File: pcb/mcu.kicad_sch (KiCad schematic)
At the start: 19 parts, among them J3 ESPPROG, J4 USB_C_Receptacle_USB2.0_14P, SW1 RST_SW, SW2 BOOT_SW, U4 ESP32-C6-MINI-1, U6 TLV803S, U7 W5500

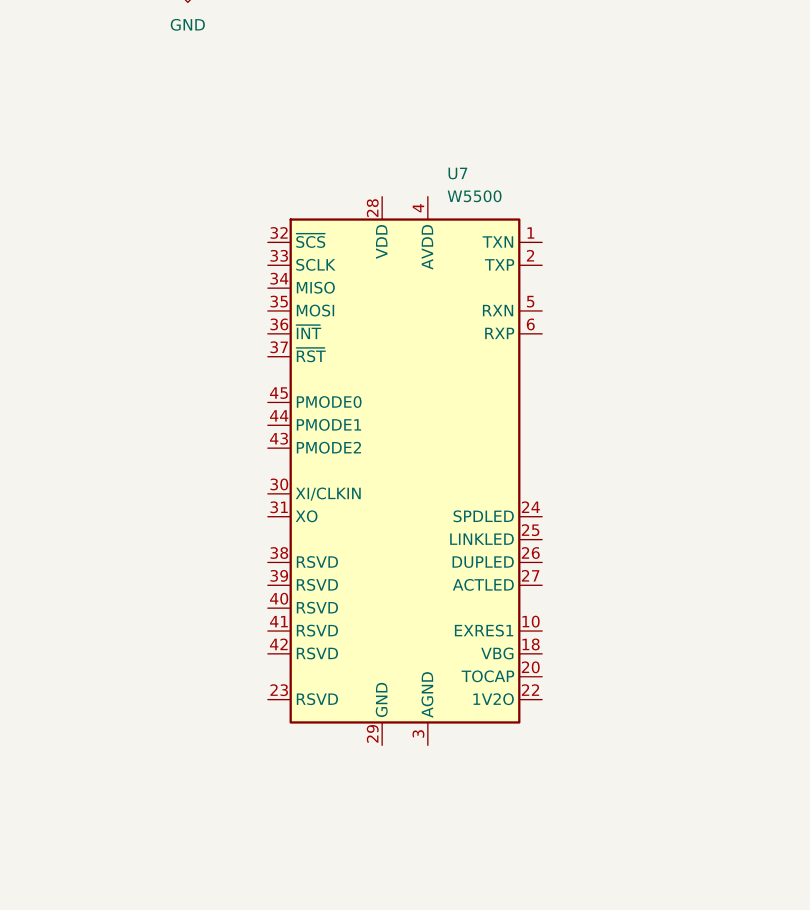
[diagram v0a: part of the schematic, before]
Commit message: feat: add W5500 ethernet controller
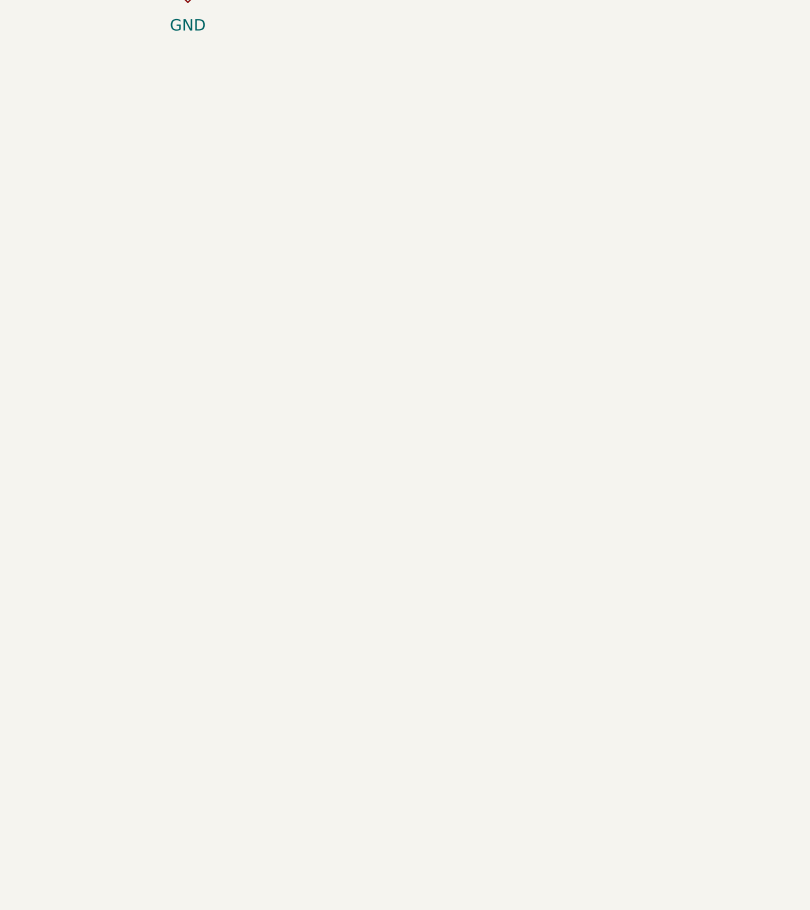
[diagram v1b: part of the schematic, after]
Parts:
- removed U7: W5500, Package_QFP:LQFP-48_7x7mm_P0.5mm, symbol Interface_Ethernet:W5500
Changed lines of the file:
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@@
-	)
-	(symbol
-		(lib_id "Interface_Ethernet:W5500")
-		(at 120.65 106.68 0)
-		(unit 1)
-		(body_style 1)
-		(exclude_from_sim no)
-		(in_bom yes)
-		(on_board yes)
-		(in_pos_files yes)
-		(dnp no)
-		(fields_autoplaced yes)
-		(property "Reference" "U7"
-			(at 125.3333 73.66 0)
-			(show_name no)
-			(do_not_autoplace no)
-			(effects
-				(font
-					(size 1.27 1.27)
-				)
-				(justify left)
-			)
-		)
-		(property "Value" "W5500"
-			(at 125.3333 76.2 0)
-			(show_name no)
-			(do_not_autoplace no)
-			(effects
-				(font
-					(size 1.27 1.27)
-				)
-				(justify left)
-			)
-		)
-		(property "Footprint" "Package_QFP:LQFP-48_7x7mm_P0.5mm"
-			(at 120.65 64.77 0)
-			(hide yes)
-			(show_name no)
-			(do_not_autoplace no)
-			(effects
-				(font
-					(size 1.27 1.27)
-				)
-			)
-		)
-		(property "Datasheet" "http://wizwiki.net/wiki/lib/exe/fetch.php/products:w5500:w5500_ds_v109e.pdf"
-			(at 120.65 81.28 0)
-			(hide yes)
-			(show_name no)
-			(do_not_autoplace no)
-			(effects
-				(font
-					(size 1.27 1.27)
-				)
-			)
-		)
-		(property "Description" "10/100Mb SPI Ethernet controller with TCP/IP stack, LQFP-48"
-			(at 120.65 106.68 0)
-			(hide yes)
-			(show_name no)
-			(do_not_autoplace no)
-			(effects
-				(font
-					(size 1.27 1.27)
-				)
-			)
-		)
-		(pin "2"
-		)
-		(pin "9"
-		)
-		(pin "38"
-		)
-		(pin "5"
-		)
-		(pin "23"
-		)
-		(pin "10"
-		)
-		(pin "26"
-		)
-		(pin "24"
-		)
-		(pin "7"
-		)
-		(pin "40"
-		)
-		(pin "8"
-		)
-		(pin "29"
-		)
-		(pin "16"
-		)
-		(pin "13"
-		)
-		(pin "25"
-		)
-		(pin "12"
-		)
-		(pin "33"
-		)
-		(pin "18"
-		)
-		(pin "14"
-		)
-		(pin "22"
-		)
-		(pin "35"
-		)
-		(pin "32"
-		)
-		(pin "46"
-		)
-		(pin "19"
-		)
-		(pin "20"
-		)
-		(pin "3"
-		)
-		(pin "30"
-		)
-		(pin "28"
-		)
-		(pin "37"
-		)
-		(pin "11"
-		)
-		(pin "17"
-		)
-		(pin "42"
-		)
-		(pin "39"
-		)
-		(pin "6"
-		)
-		(pin "43"
-		)
-		(pin "31"
-		)
-		(pin "44"
-		)
-		(pin "27"
-		)
-		(pin "15"
-		)
-		(pin "34"
-		)
-		(pin "48"
-		)
-		(pin "47"
-		)
-		(pin "1"
-		)
-		(pin "41"
-		)
-		(pin "45"
-		)
-		(pin "21"
-		)
-		(pin "36"
-		)
-		(pin "4"
-		)
-		(instances
-			(project "EveningStar"
-				(path "/4c61f5a2-f8d4-462a-9bc3-d74437d30372/83e90eda-4c3c-4f86-9f5b-c472ac53896a"
-					(reference "U7")
-					(unit 1)
-				)
-			)
-		)
 	)
 	(symbol

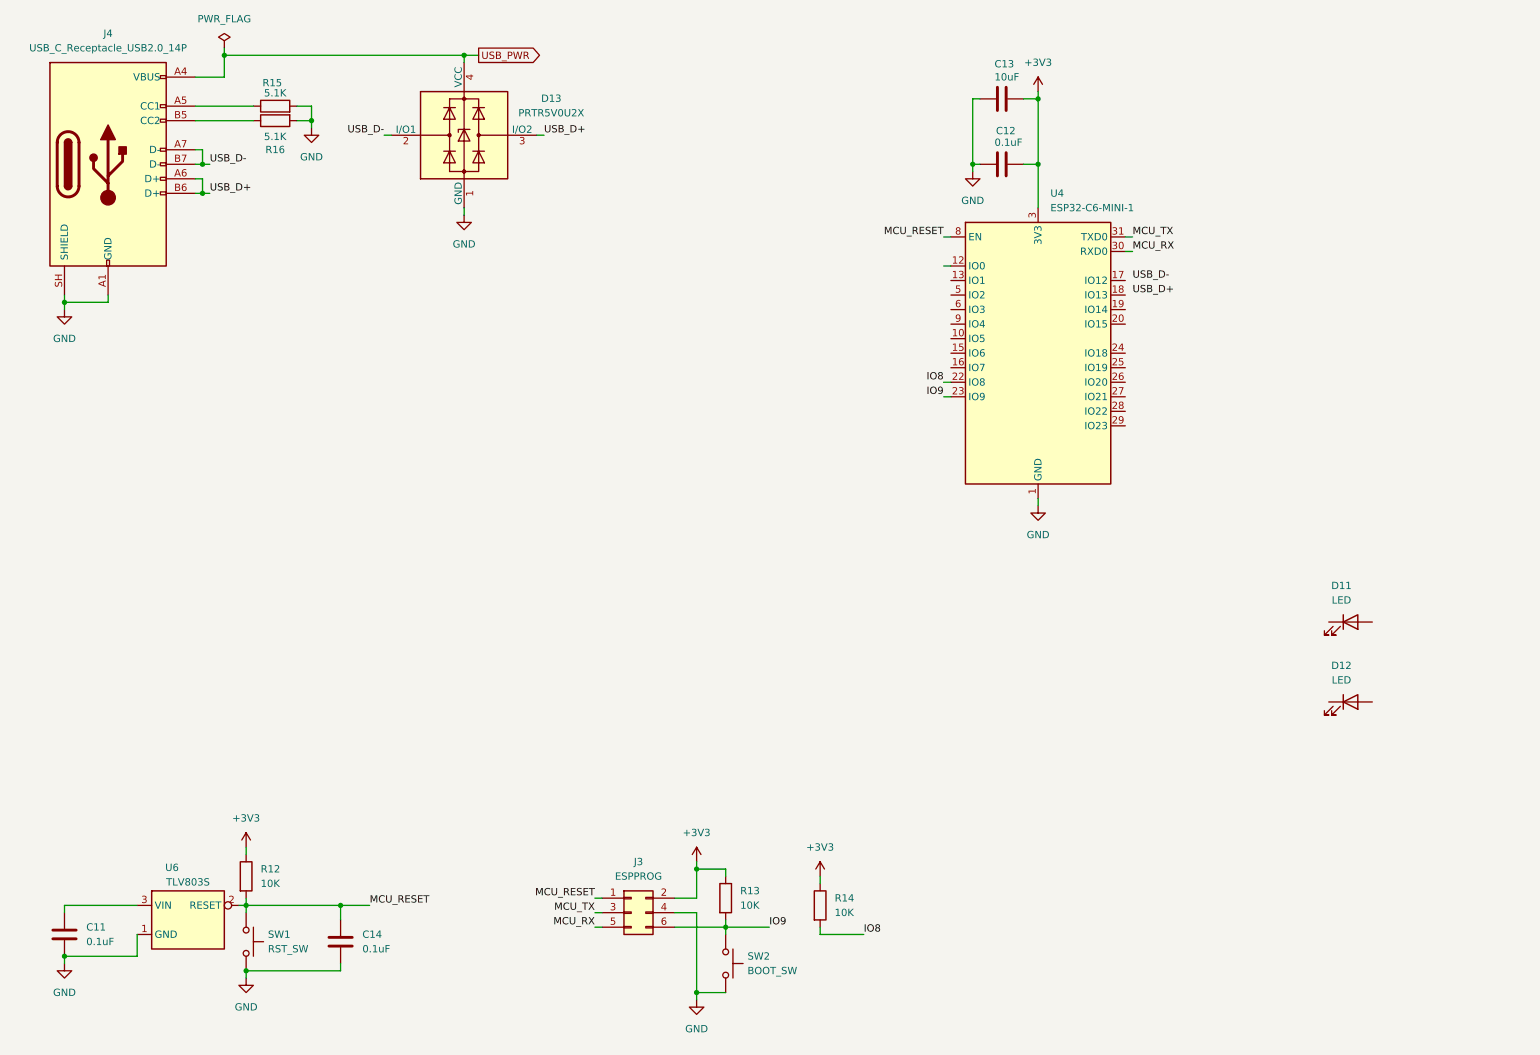
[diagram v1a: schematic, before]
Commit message: feat: connect ethernet to mcu and sort erc errors
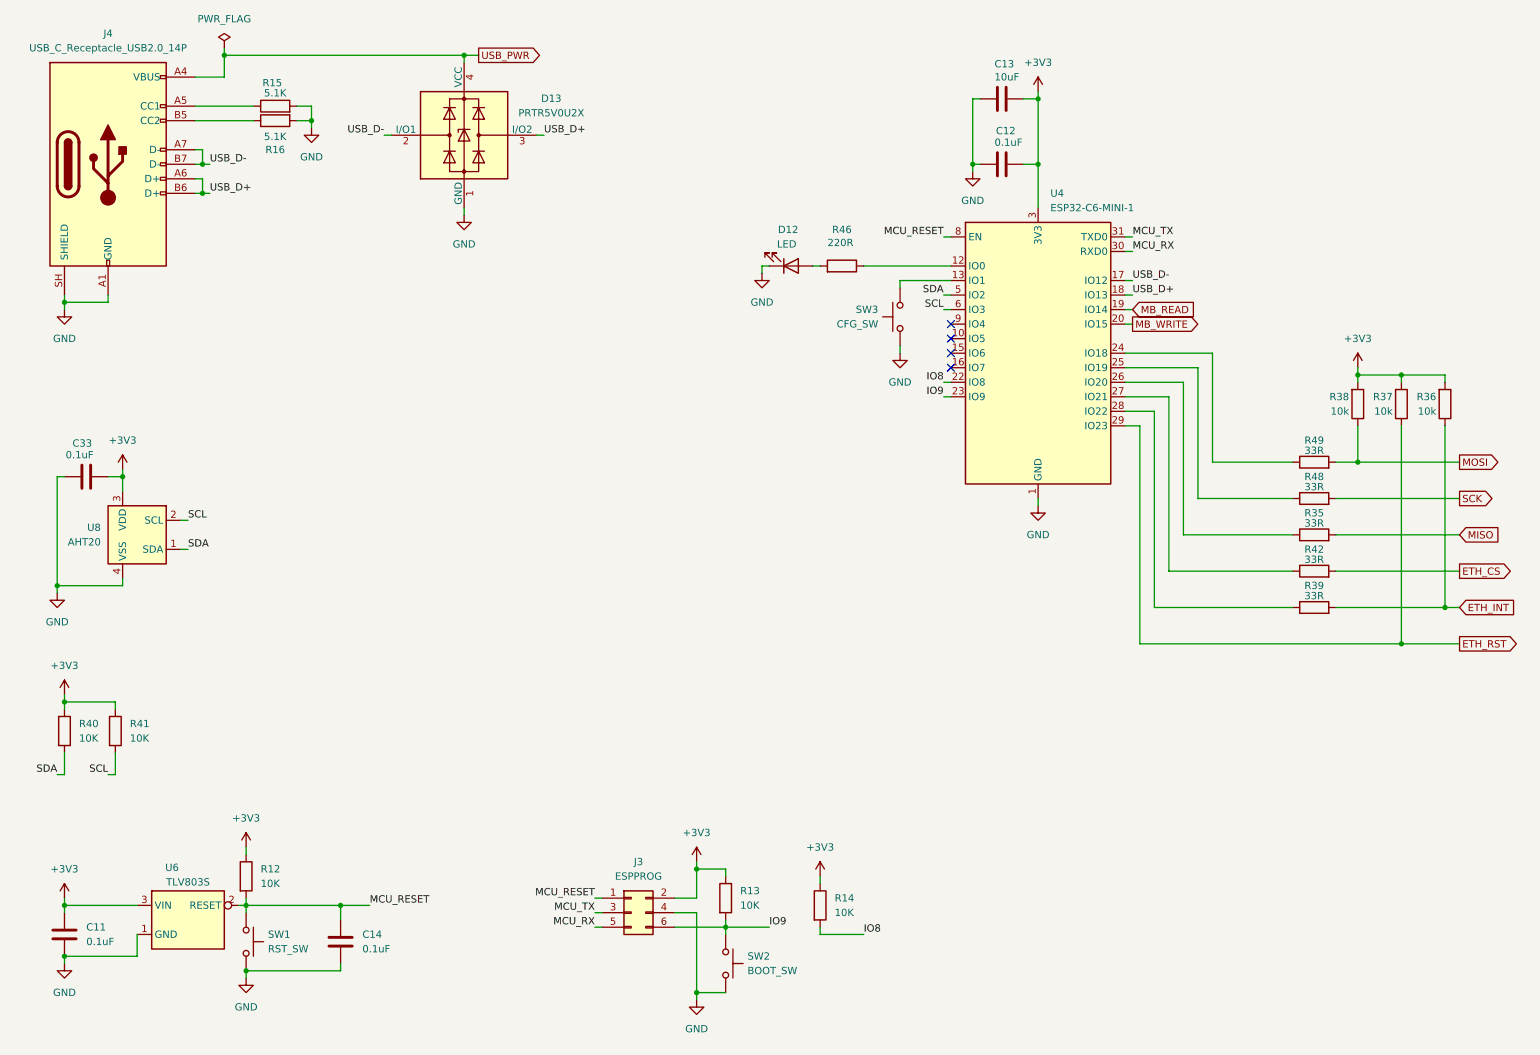
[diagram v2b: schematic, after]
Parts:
- removed D11: LED, symbol Device:LED
- added C33: 0.1uF, symbol Device:C
- added R35, R39, R42, R48, R49: 33R, symbol Device:R
- added R36, R37, R38: 10k, symbol Device:R
- added R40, R41: 10K, symbol Device:R
- added R46: 220R, symbol Device:R
- added SW3: CFG_SW, symbol Switch:SW_Push
- added U8: AHT20, symbol custom_symbols:AHT20
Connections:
- net +3V3: now also C11.1, U6.3 (VIN), C33.2, R36.2, R37.2, R38.2, R40.1, R41.1, U8.3 (VDD)
- net GND: now also D12.1 (K), C33.1, SW3.2, U8.4 (VSS)
- net USB_D+: now also U4.18 (IO13)
- net USB_D-: now also U4.17 (IO12)
- net at U4.12 (IO0): now also R46.1
- net at U4.13 (IO1): now also SW3.1
- net MB_READ: now reaches U4.19 (IO14)
- net MB_WRITE: now reaches U4.20 (IO15)
- net at U4.24 (IO18): now also R49.1
- net at U4.25 (IO19): now also R48.1
- net at U4.26 (IO20): now also R35.1
- net at U4.27 (IO21): now also R42.1
- net at U4.28 (IO22): now also R39.1
- net ETH_RST: now reaches U4.29 (IO23)
- net ETH_RST: now also R37.1
- net SDA: now reaches U4.5 (IO2)
- net SDA: now also R40.2, U8.1 (SDA)
- net SCL: now reaches U4.6 (IO3)
- net SCL: now also R41.2, U8.2 (SCL)
- net at D12.2 (A): now also R46.2
- new net ETH_CS: R42.2
- new net ETH_INT: R36.1, R39.2
- new net MISO: R35.2
- new net MOSI: R38.1, R49.2
- new net SCK: R48.2
- no-connect marks 0 -> 4

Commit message: feat: update compoents with lcsc parts
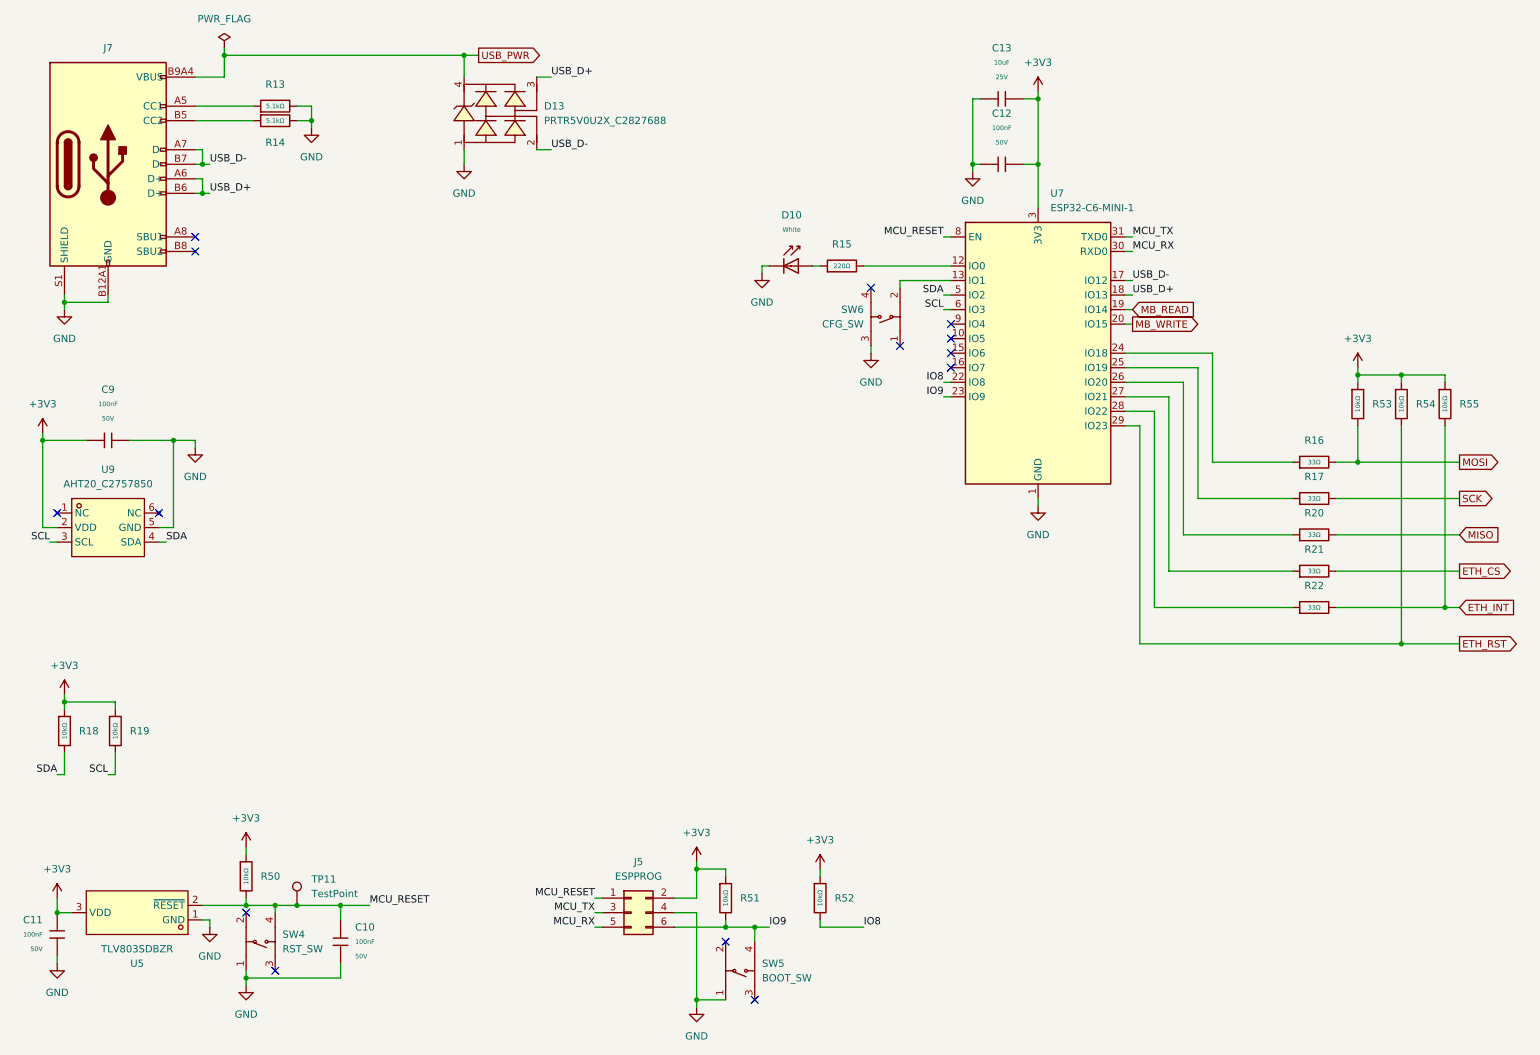
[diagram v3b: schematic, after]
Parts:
- removed C11, C12, C14, C33: 0.1uF, symbol Device:C
- removed C13: 10uF, symbol Device:C
- removed D12: LED, symbol Device:LED
- removed D13: PRTR5V0U2X, Package_TO_SOT_SMD:SOT-143, symbol Power_Protection:PRTR5V0U2X
- removed J4: USB_C_Receptacle_USB2.0_14P, symbol Connector:USB_C_Receptacle_USB2.0_14P
- removed R12, R13, R14, R40, R41: 10K, symbol Device:R
- removed R15, R16: 5.1K, symbol Device:R
- removed R35, R39, R42, R48, R49: 33R, symbol Device:R
- removed R36, R37, R38: 10k, symbol Device:R
- removed R46: 220R, symbol Device:R
- removed SW1: RST_SW, symbol Switch:SW_Push
- removed SW2: BOOT_SW, symbol Switch:SW_Push
- removed SW3: CFG_SW, symbol Switch:SW_Push
- removed U6: TLV803S, Package_TO_SOT_SMD:SOT-23, symbol custom_symbols:TLV803S
- removed U8: AHT20, symbol custom_symbols:AHT20
- added C10, C11, C12, C9: 100nF, PCM_JLCPCB:C_0603, symbol PCM_JLCPCB-Capacitors:0603,100nF
- added C13: 10uF, PCM_JLCPCB:C_0603, symbol PCM_JLCPCB-Capacitors:0603,10uF,(2)
- added D10: White, PCM_JLCPCB:D_0805, symbol PCM_JLCPCB-Diodes:LED,0805,White
- added D13: PRTR5V0U2X_C2827688, EasyEDA:SOT-143-4_L2.9-W1.3-P1.92-LS2.4-BL, symbol EasyEDA:PRTR5V0U2X_C2827688
- added J7: Connector, USB-TYPE-C-16P, PCM_JLCPCB:TYPE-C-SMD_HX-TYPE-C-16PIN, symbol PCM_JLCPCB-Extended:Connector, USB-TYPE-C-16P
- added R13, R14: 5.1kΩ, PCM_JLCPCB:R_0603, symbol PCM_JLCPCB-Resistors:0603,5.1kΩ
- added R15: 220Ω, PCM_JLCPCB:R_0603, symbol PCM_JLCPCB-Resistors:0603,220Ω
- added R16, R17, R20, R21, R22: 33Ω, PCM_JLCPCB:R_0603, symbol PCM_JLCPCB-Resistors:0603,33Ω
- added R18, R19, R50, R51, R52, R53, R54, R55: 10kΩ, PCM_JLCPCB:R_0603, symbol PCM_JLCPCB-Resistors:0603,10kΩ
- added SW4: RST_SW, EasyEDA:KEY-SMD_4P-L6.0-W6.0-P3.90-LS9.0, symbol EasyEDA:TS-1095PS-A1B2-C3D2
- added SW5: BOOT_SW, EasyEDA:KEY-SMD_4P-L6.0-W6.0-P3.90-LS9.0, symbol EasyEDA:TS-1095PS-A1B2-C3D2
- added SW6: CFG_SW, EasyEDA:KEY-SMD_4P-L6.0-W6.0-P3.90-LS9.0, symbol EasyEDA:TS-1095PS-A1B2-C3D2
- added TP11: TestPoint, EasyEDA:TEST-TH_BD2.54-P1.4_BLACK, symbol Connector:TestPoint
- added U5: TLV803SDBZR, EasyEDA:SOT-23-3_L2.9-W1.3-P1.90-LS2.4-BR, symbol EasyEDA:TLV803SDBZR
- added U9: AHT20_C2757850, EasyEDA:SENSOR-SMD_L3.0-W3.0-P1.00-BR, symbol EasyEDA:AHT20_C2757850
- J5: renamed from J3; footprint (none) -> EasyEDA:IDC-TH_6P-P2.54-V-R2-C3-S2.54; LCSC Part (none) -> C492441; MPN (none) -> BH254V-6P
- U7: renamed from U4; footprint RF_Module:ESP32-C6-MINI-1 -> EasyEDA:WIFIM-SMD_61P-L16.6-W13.2-P0.80-ESP32-C6-MINI-1-N4; LCSC Part (none) -> C5736265; MPN (none) -> ESP32-C6-MINI-1-N4
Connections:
- net +3V3: now also C11.2, C12.1, C13.2, C9.1, R18.1, R19.1, R50.1, R51.1, R52.1, R53.1, R54.1, R55.1, U5.3 (VDD), U9.2 (VDD)
- net ETH_CS: now also R21.2
- net ETH_INT: now also R22.2, R55.2
- net ETH_RST: now also R54.2
- net GND: now also C10.1, C11.1, C12.2, C13.1, C9.2, D10.1, D13.1, J7.A12B1 (GND), J7.B12A1 (GND), J7.S1 (SHIELD), R13.2, R14.2, SW4.1, SW5.1, SW6.3, U5.1 (GND), U9.5 (GND)
- net IO8: now also R52.2
- net IO9: now also R51.2, SW5.4
- net MCU_RESET: now also C10.2, R50.2, SW4.4, TP11.1, U5.2 (~{RESET})
- net MISO: now also R20.2
- net MOSI: now also R16.2, R53.2
- net SCK: now also R17.2
- net SCL: now also R19.2, U9.3 (SCL)
- net SDA: now also R18.2, U9.4 (SDA)
- net USB_D+: now also D13.3, J7.A6 (D+), J7.B6 (D+)
- net USB_D-: now also D13.2, J7.A7 (D-), J7.B7 (D-)
- net USB_PWR: now also D13.4, J7.A9B4 (VBUS), J7.B9A4 (VBUS)
- net at U7.28 (IO22): now also R22.1
- net at U7.12 (IO0): now also R15.2
- net at U7.13 (IO1): now also SW6.2
- net at U7.24 (IO18): now also R16.1
- net at U7.25 (IO19): now also R17.1
- net at U7.26 (IO20): now also R20.1
- net at U7.27 (IO21): now also R21.1
- new net: J7.B5 (CC2), R14.1
- new net: J7.A5 (CC1), R13.1
- new net: D10.2, R15.1
- no-connect marks 4 -> 14

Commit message: feat: layout meterbus frontend
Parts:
- renumbered C11 to C12, C9 to C13, C10 to C14, C13 to C15, C12 to C16, D13 to D11, D10 to D12, J7 to J2, J5 to J3, R18 to R15, R19 to R16, R50 to R17, R13 to R18, R14 to R19, R51 to R20, R52 to R21, R15 to R22, R16 to R23, R17 to R24, R20 to R25, R21 to R26, R22 to R27, R53 to R28, R54 to R29, R55 to R30, SW4 to SW1, SW5 to SW2, SW6 to SW3, U9 to U6, U5 to U7, U7 to U8

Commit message: feat: roughly lay out mcu
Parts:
- added TP18: MOSI, TestPoint:TestPoint_Pad_1.5x1.5mm, symbol Connector:TestPoint
- added TP19: SCK, TestPoint:TestPoint_Pad_1.5x1.5mm, symbol Connector:TestPoint
- added TP20: MISO, TestPoint:TestPoint_Pad_1.5x1.5mm, symbol Connector:TestPoint
- added TP21: ETH_CS, TestPoint:TestPoint_Pad_1.5x1.5mm, symbol Connector:TestPoint
- added TP22: ETH_INT, TestPoint:TestPoint_Pad_1.5x1.5mm, symbol Connector:TestPoint
- added TP23: ETH_RST, TestPoint:TestPoint_Pad_1.5x1.5mm, symbol Connector:TestPoint
- TP11: value TestPoint -> MCU_RST
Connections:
- net ETH_CS: now also TP21.1
- net ETH_INT: now also TP22.1
- net ETH_RST: now also TP23.1
- net MISO: now also TP20.1
- net MOSI: now also TP18.1
- net SCK: now also TP19.1
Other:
- moved on the sheet: R23, R24, R25, R26, R27

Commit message: feat: layout psu and rest of mcu
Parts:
- TP18, TP19, TP20, TP21, TP22, TP23: footprint TestPoint:TestPoint_Pad_1.5x1.5mm -> TestPoint:TestPoint_Pad_1.0x1.0mm
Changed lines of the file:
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@@
 			)
 		)
-		(property "Footprint" "TestPoint:TestPoint_Pad_1.5x1.5mm"
+		(property "Footprint" "TestPoint:TestPoint_Pad_1.0x1.0mm"
 			(at 246.38 114.3 0)
 			(hide yes)
@@
 			)
 		)
-		(property "Footprint" "TestPoint:TestPoint_Pad_1.5x1.5mm"
+		(property "Footprint" "TestPoint:TestPoint_Pad_1.0x1.0mm"
 			(at 246.38 95.25 0)
 			(hide yes)
@@
 			)
 		)
-		(property "Footprint" "TestPoint:TestPoint_Pad_1.5x1.5mm"
+		(property "Footprint" "TestPoint:TestPoint_Pad_1.0x1.0mm"
 			(at 246.38 127 0)
 			(hide yes)
@@
 			)
 		)
-		(property "Footprint" "TestPoint:TestPoint_Pad_1.5x1.5mm"
+		(property "Footprint" "TestPoint:TestPoint_Pad_1.0x1.0mm"
 			(at 246.38 101.6 0)
 			(hide yes)
@@
 			)
 		)
-		(property "Footprint" "TestPoint:TestPoint_Pad_1.5x1.5mm"
+		(property "Footprint" "TestPoint:TestPoint_Pad_1.0x1.0mm"
 			(at 246.38 107.95 0)
 			(hide yes)
@@
 			)
 		)
-		(property "Footprint" "TestPoint:TestPoint_Pad_1.5x1.5mm"
+		(property "Footprint" "TestPoint:TestPoint_Pad_1.0x1.0mm"
 			(at 246.38 120.65 0)
 			(hide yes)
